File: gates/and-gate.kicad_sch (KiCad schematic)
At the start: 5 parts

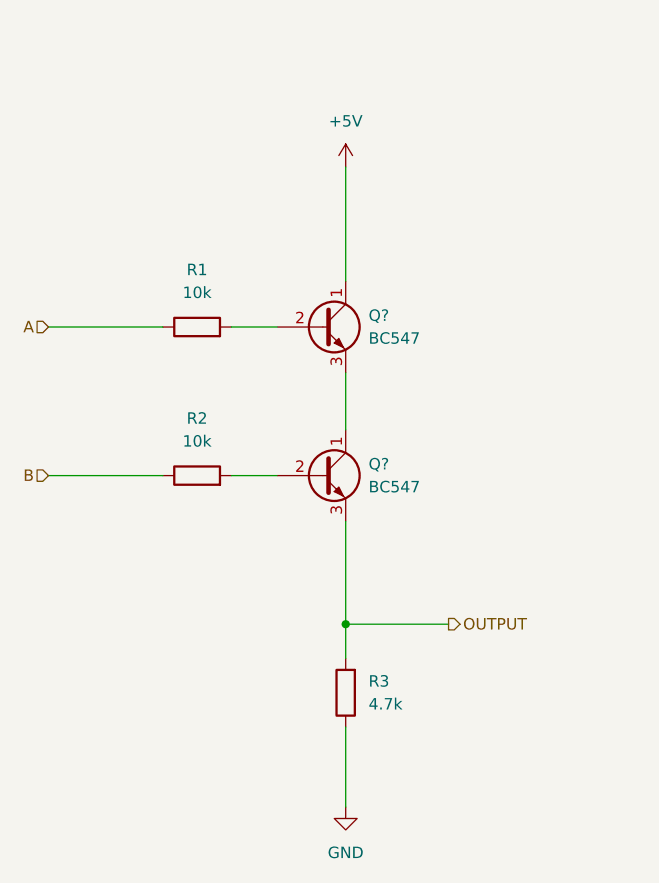
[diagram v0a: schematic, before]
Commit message: replaced circuitry in half adder with reusable gates
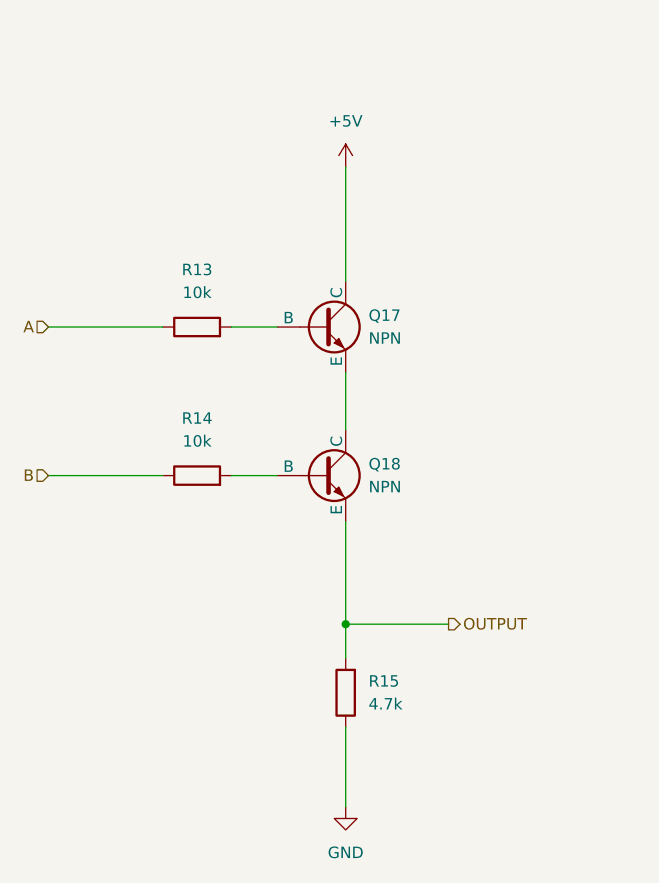
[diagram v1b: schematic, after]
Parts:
- removed Q? (x2): BC547, Package_TO_SOT_THT:TO-92_Inline, symbol Transistor_BJT:BC547
- added Q17, Q18: NPN, symbol Simulation_SPICE:NPN
- renumbered R1 to R13, R2 to R14, R3 to R15
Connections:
- net +5V: now also Q17.1 (C)
- net OUTPUT: now also Q18.3 (E)
- net at R13.2: now also Q17.2 (B)
- net at R14.2: now also Q18.2 (B)
- new net: Q17.3 (E), Q18.1 (C)

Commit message: Clock project
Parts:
- renumbered R13 to R28, R14 to R29, R15 to R30
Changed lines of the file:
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@@
 		(dnp no)
 		(fields_autoplaced yes)
-		(property "Reference" "R15"
+		(property "Reference" "R30"
 			(at 115.57 111.7599 0)
 			(effects
@@
 				(path "/88c27409-0a88-4cf1-8b65-cf7271709e32/c6fa08ba-c5fb-43d8-850f-3e5322725fc3/84309def-b1d1-4d08-9cf0-44a7dcd7d6e9"
 					(reference "R24")
+					(unit 1)
+				)
+			)
+			(project "half-adder"
+				(path "/aa2ffd02-03c7-43f5-905d-233d00be0633/8e657cf9-09ea-4d19-97ba-111b741f01c5/84309def-b1d1-4d08-9cf0-44a7dcd7d6e9"
+					(reference "R30")
 					(unit 1)
 				)
@@
 		(dnp no)
 		(fields_autoplaced yes)
-		(property "Reference" "R14"
+		(property "Reference" "R29"
 			(at 96.52 82.55 90)
 			(effects
@@
 				(path "/88c27409-0a88-4cf1-8b65-cf7271709e32/c6fa08ba-c5fb-43d8-850f-3e5322725fc3/84309def-b1d1-4d08-9cf0-44a7dcd7d6e9"
 					(reference "R23")
+					(unit 1)
+				)
+			)
+			(project "half-adder"
+				(path "/aa2ffd02-03c7-43f5-905d-233d00be0633/8e657cf9-09ea-4d19-97ba-111b741f01c5/84309def-b1d1-4d08-9cf0-44a7dcd7d6e9"
+					(reference "R29")
 					(unit 1)
 				)
@@
 		(dnp no)
 		(fields_autoplaced yes)
-		(property "Reference" "#PWR022"
+		(property "Reference" "#PWR032"
 			(at 113.03 132.08 0)
 			(effects
@@
 				(path "/88c27409-0a88-4cf1-8b65-cf7271709e32/c6fa08ba-c5fb-43d8-850f-3e5322725fc3/84309def-b1d1-4d08-9cf0-44a7dcd7d6e9"
 					(reference "#PWR028")
+					(unit 1)
+				)
+			)
+			(project "half-adder"
+				(path "/aa2ffd02-03c7-43f5-905d-233d00be0633/8e657cf9-09ea-4d19-97ba-111b741f01c5/84309def-b1d1-4d08-9cf0-44a7dcd7d6e9"
+					(reference "#PWR032")
 					(unit 1)
 				)
@@
 				)
 			)
+			(project "half-adder"
+				(path "/aa2ffd02-03c7-43f5-905d-233d00be0633/8e657cf9-09ea-4d19-97ba-111b741f01c5/84309def-b1d1-4d08-9cf0-44a7dcd7d6e9"
+					(reference "Q17")
+					(unit 1)
+				)
+			)
 		)
 	)
@@
 		(dnp no)
 		(fields_autoplaced yes)
-		(property "Reference" "R13"
+		(property "Reference" "R28"
 			(at 96.52 66.04 90)
 			(effects
@@
 				(path "/88c27409-0a88-4cf1-8b65-cf7271709e32/c6fa08ba-c5fb-43d8-850f-3e5322725fc3/84309def-b1d1-4d08-9cf0-44a7dcd7d6e9"
 					(reference "R22")
+					(unit 1)
+				)
+			)
+			(project "half-adder"
+				(path "/aa2ffd02-03c7-43f5-905d-233d00be0633/8e657cf9-09ea-4d19-97ba-111b741f01c5/84309def-b1d1-4d08-9cf0-44a7dcd7d6e9"
+					(reference "R28")
 					(unit 1)
 				)
@@
 		(dnp no)
 		(fields_autoplaced yes)
-		(property "Reference" "#PWR021"
+		(property "Reference" "#PWR031"
 			(at 113.03 58.42 0)
 			(effects
@@
 				(path "/88c27409-0a88-4cf1-8b65-cf7271709e32/c6fa08ba-c5fb-43d8-850f-3e5322725fc3/84309def-b1d1-4d08-9cf0-44a7dcd7d6e9"
 					(reference "#PWR027")
+					(unit 1)
+				)
+			)
+			(project "half-adder"
+				(path "/aa2ffd02-03c7-43f5-905d-233d00be0633/8e657cf9-09ea-4d19-97ba-111b741f01c5/84309def-b1d1-4d08-9cf0-44a7dcd7d6e9"
+					(reference "#PWR031")
 					(unit 1)
 				)
@@
 					(unit 1)
 				)
+			)
+			(project "half-adder"
+				(path "/aa2ffd02-03c7-43f5-905d-233d00be0633/8e657cf9-09ea-4d19-97ba-111b741f01c5/84309def-b1d1-4d08-9cf0-44a7dcd7d6e9"
+					(reference "Q18")
+					(unit 1)
+				)

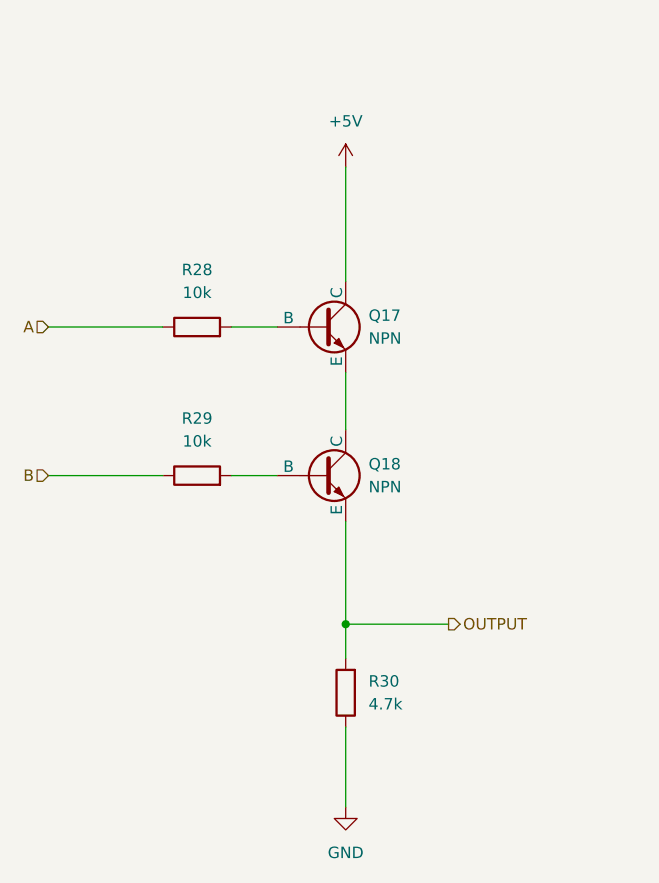
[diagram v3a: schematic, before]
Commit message: Fixed gates and moved half adder to its own directory
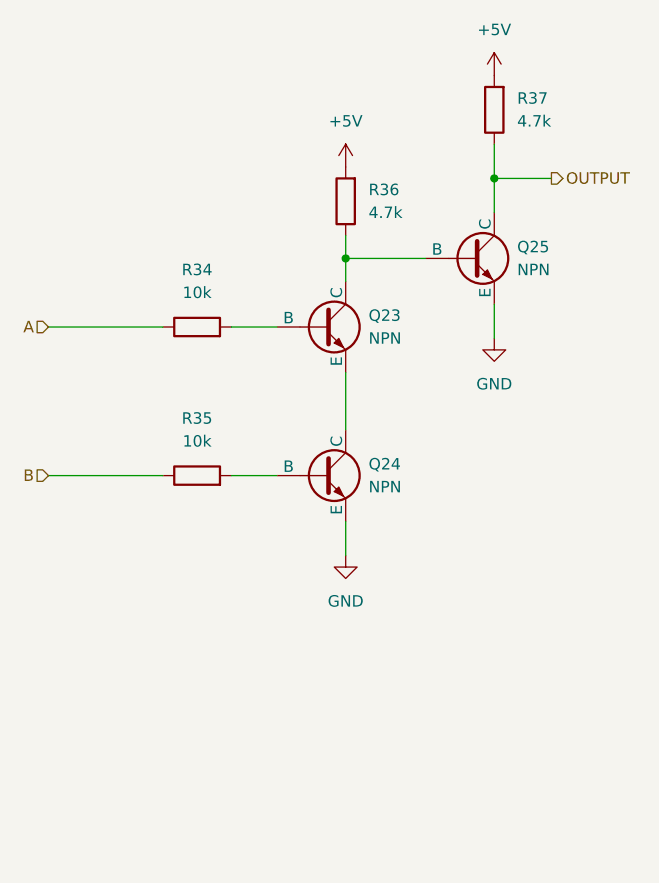
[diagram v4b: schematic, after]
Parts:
- removed R30: 4.7k, symbol Device:R
- added Q25: NPN, symbol Simulation_SPICE:NPN
- added R36, R37: 4.7k, symbol Device:R
- renumbered Q17 to Q23, Q18 to Q24, R28 to R34, R29 to R35
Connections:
- net +5V: now also R36.2, R37.2; no longer Q23.1 (C)
- net GND: now also Q24.3 (E), Q25.3 (E)
- net OUTPUT: now also Q25.1 (C), R37.1; no longer Q24.3 (E)
- new net: Q23.1 (C), Q25.2 (B), R36.1

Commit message: Schematic for register
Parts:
- renumbered Q23 to Q2, Q24 to Q3, Q25 to Q4, R34 to R3, R35 to R4, R36 to R5, R37 to R6
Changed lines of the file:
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@@
 		(dnp no)
 		(fields_autoplaced yes)
-		(property "Reference" "R37"
+		(property "Reference" "R6"
 			(at 132.08 46.9899 0)
 			(effects
@@
 		)
 		(instances
+			(project "register"
+				(path "/176ebc34-d92d-46b0-a9f1-4fb76aa55196/2b210005-c9ef-43dd-bd20-4304cf65b93c/50b17f16-b17e-4be7-91be-701141deb920"
+					(reference "R6")
+					(unit 1)
+				)
+				(path "/176ebc34-d92d-46b0-a9f1-4fb76aa55196/2b210005-c9ef-43dd-bd20-4304cf65b93c/88ab6d81-8ed2-43ff-9a30-e648785f4c69"
+					(reference "R6")
+					(unit 1)
+				)
+			)
 			(project "half-adder"
 				(path "/88c27409-0a88-4cf1-8b65-cf7271709e32/67fd5552-853b-444b-a1e8-d0b78302ff23"
@@
 		(dnp no)
 		(fields_autoplaced yes)
-		(property "Reference" "R35"
+		(property "Reference" "R4"
 			(at 96.52 82.55 90)
 			(effects
@@
 		)
 		(instances
+			(project "register"
+				(path "/176ebc34-d92d-46b0-a9f1-4fb76aa55196/2b210005-c9ef-43dd-bd20-4304cf65b93c/50b17f16-b17e-4be7-91be-701141deb920"
+					(reference "R4")
+					(unit 1)
+				)
+				(path "/176ebc34-d92d-46b0-a9f1-4fb76aa55196/2b210005-c9ef-43dd-bd20-4304cf65b93c/88ab6d81-8ed2-43ff-9a30-e648785f4c69"
+					(reference "R4")
+					(unit 1)
+				)
+			)
 			(project "half-adder"
 				(path "/88c27409-0a88-4cf1-8b65-cf7271709e32/67fd5552-853b-444b-a1e8-d0b78302ff23"
@@
 		(dnp no)
 		(fields_autoplaced yes)
-		(property "Reference" "#PWR044"
+		(property "Reference" "#PWR04"
 			(at 113.03 104.14 0)
 			(effects
@@
 		)
 		(instances
+			(project "register"
+				(path "/176ebc34-d92d-46b0-a9f1-4fb76aa55196/2b210005-c9ef-43dd-bd20-4304cf65b93c/50b17f16-b17e-4be7-91be-701141deb920"
+					(reference "#PWR04")
+					(unit 1)
+				)
+				(path "/176ebc34-d92d-46b0-a9f1-4fb76aa55196/2b210005-c9ef-43dd-bd20-4304cf65b93c/88ab6d81-8ed2-43ff-9a30-e648785f4c69"
+					(reference "#PWR04")
+					(unit 1)
+				)
+			)
 			(project "half-adder"
 				(path "/88c27409-0a88-4cf1-8b65-cf7271709e32/67fd5552-853b-444b-a1e8-d0b78302ff23"
-					(reference "#PWR044")
+					(reference "#PWR042")
 					(unit 1)
 				)
 				(path "/88c27409-0a88-4cf1-8b65-cf7271709e32/e853c8d3-eefb-4fd9-b6d3-3d5bff45301a"
-					(reference "#PWR040")
+					(reference "#PWR038")
 					(unit 1)
 				)
 				(path "/88c27409-0a88-4cf1-8b65-cf7271709e32/9ae6b3ee-29f0-4a20-9e44-32b28e8d9225/84309def-b1d1-4d08-9cf0-44a7dcd7d6e9"
-					(reference "#PWR026")
+					(reference "#PWR024")
 					(unit 1)
 				)
 				(path "/88c27409-0a88-4cf1-8b65-cf7271709e32/c6fa08ba-c5fb-43d8-850f-3e5322725fc3/84309def-b1d1-4d08-9cf0-44a7dcd7d6e9"
-					(reference "#PWR036")
+					(reference "#PWR034")
 					(unit 1)
 				)
@@
 		(dnp no)
 		(fields_autoplaced yes)
-		(property "Reference" "Q23"
+		(property "Reference" "Q2"
 			(at 115.57 71.1199 0)
 			(effects
@@
 		)
 		(instances
+			(project "register"
+				(path "/176ebc34-d92d-46b0-a9f1-4fb76aa55196/2b210005-c9ef-43dd-bd20-4304cf65b93c/50b17f16-b17e-4be7-91be-701141deb920"
+					(reference "Q2")
+					(unit 1)
+				)
+				(path "/176ebc34-d92d-46b0-a9f1-4fb76aa55196/2b210005-c9ef-43dd-bd20-4304cf65b93c/88ab6d81-8ed2-43ff-9a30-e648785f4c69"
+					(reference "Q2")
+					(unit 1)
+				)
+			)
 			(project "half-adder"
 				(path "/88c27409-0a88-4cf1-8b65-cf7271709e32/67fd5552-853b-444b-a1e8-d0b78302ff23"
@@
 		(dnp no)
 		(fields_autoplaced yes)
-		(property "Reference" "#PWR046"
+		(property "Reference" "#PWR06"
 			(at 129.54 80.01 0)
 			(effects
@@
 		)
 		(instances
+			(project "register"
+				(path "/176ebc34-d92d-46b0-a9f1-4fb76aa55196/2b210005-c9ef-43dd-bd20-4304cf65b93c/50b17f16-b17e-4be7-91be-701141deb920"
+					(reference "#PWR06")
+					(unit 1)
+				)
+				(path "/176ebc34-d92d-46b0-a9f1-4fb76aa55196/2b210005-c9ef-43dd-bd20-4304cf65b93c/88ab6d81-8ed2-43ff-9a30-e648785f4c69"
+					(reference "#PWR06")
+					(unit 1)
+				)
+			)
 			(project "half-adder"
 				(path "/88c27409-0a88-4cf1-8b65-cf7271709e32/67fd5552-853b-444b-a1e8-d0b78302ff23"
-					(reference "#PWR046")
+					(reference "#PWR044")
 					(unit 1)
 				)
 				(path "/88c27409-0a88-4cf1-8b65-cf7271709e32/e853c8d3-eefb-4fd9-b6d3-3d5bff45301a"
-					(reference "#PWR042")
+					(reference "#PWR040")
 					(unit 1)
 				)
 				(path "/88c27409-0a88-4cf1-8b65-cf7271709e32/9ae6b3ee-29f0-4a20-9e44-32b28e8d9225/84309def-b1d1-4d08-9cf0-44a7dcd7d6e9"
-					(reference "#PWR028")
+					(reference "#PWR026")
 					(unit 1)
 				)
 				(path "/88c27409-0a88-4cf1-8b65-cf7271709e32/c6fa08ba-c5fb-43d8-850f-3e5322725fc3/84309def-b1d1-4d08-9cf0-44a7dcd7d6e9"
-					(reference "#PWR038")
+					(reference "#PWR036")
 					(unit 1)
 				)
@@
 		(dnp no)
 		(fields_autoplaced yes)
-		(property "Reference" "Q25"
+		(property "Reference" "Q4"
 			(at 132.08 63.4999 0)
 			(effects
@@
 		)
 		(instances
+			(project "register"
+				(path "/176ebc34-d92d-46b0-a9f1-4fb76aa55196/2b210005-c9ef-43dd-bd20-4304cf65b93c/50b17f16-b17e-4be7-91be-701141deb920"
+					(reference "Q4")
+					(unit 1)
+				)
+				(path "/176ebc34-d92d-46b0-a9f1-4fb76aa55196/2b210005-c9ef-43dd-bd20-4304cf65b93c/88ab6d81-8ed2-43ff-9a30-e648785f4c69"
+					(reference "Q4")
+					(unit 1)
+				)
+			)
 			(project "half-adder"
 				(path "/88c27409-0a88-4cf1-8b65-cf7271709e32/67fd5552-853b-444b-a1e8-d0b78302ff23"
@@
 		(dnp no)
 		(fields_autoplaced yes)
-		(property "Reference" "R34"
+		(property "Reference" "R3"
 			(at 96.52 66.04 90)
 			(effects
@@
 		)
 		(instances
+			(project "register"
+				(path "/176ebc34-d92d-46b0-a9f1-4fb76aa55196/2b210005-c9ef-43dd-bd20-4304cf65b93c/50b17f16-b17e-4be7-91be-701141deb920"
+					(reference "R3")
+					(unit 1)
+				)
+				(path "/176ebc34-d92d-46b0-a9f1-4fb76aa55196/2b210005-c9ef-43dd-bd20-4304cf65b93c/88ab6d81-8ed2-43ff-9a30-e648785f4c69"
+					(reference "R3")
+					(unit 1)
+				)
+			)
 			(project "half-adder"
 				(path "/88c27409-0a88-4cf1-8b65-cf7271709e32/67fd5552-853b-444b-a1e8-d0b78302ff23"
@@
 		(dnp no)
 		(fields_autoplaced yes)
-		(property "Reference" "#PWR045"
+		(property "Reference" "#PWR05"
 			(at 129.54 48.26 0)
 			(effects
@@
 		)
 		(instances
+			(project "register"
+				(path "/176ebc34-d92d-46b0-a9f1-4fb76aa55196/2b210005-c9ef-43dd-bd20-4304cf65b93c/50b17f16-b17e-4be7-91be-701141deb920"
+					(reference "#PWR05")
+					(unit 1)
+				)
+				(path "/176ebc34-d92d-46b0-a9f1-4fb76aa55196/2b210005-c9ef-43dd-bd20-4304cf65b93c/88ab6d81-8ed2-43ff-9a30-e648785f4c69"
+					(reference "#PWR05")
+					(unit 1)
+				)
+			)
 			(project "half-adder"
 				(path "/88c27409-0a88-4cf1-8b65-cf7271709e32/67fd5552-853b-444b-a1e8-d0b78302ff23"
-					(reference "#PWR045")
+					(reference "#PWR043")
 					(unit 1)
 				)
 				(path "/88c27409-0a88-4cf1-8b65-cf7271709e32/e853c8d3-eefb-4fd9-b6d3-3d5bff45301a"
-					(reference "#PWR041")
+					(reference "#PWR039")
 					(unit 1)
 				)
 				(path "/88c27409-0a88-4cf1-8b65-cf7271709e32/9ae6b3ee-29f0-4a20-9e44-32b28e8d9225/84309def-b1d1-4d08-9cf0-44a7dcd7d6e9"
-					(reference "#PWR027")
+					(reference "#PWR025")
 					(unit 1)
 				)
 				(path "/88c27409-0a88-4cf1-8b65-cf7271709e32/c6fa08ba-c5fb-43d8-850f-3e5322725fc3/84309def-b1d1-4d08-9cf0-44a7dcd7d6e9"
-					(reference "#PWR037")
+					(reference "#PWR035")
 					(unit 1)
 				)
@@
 		(dnp no)
 		(fields_autoplaced yes)
-		(property "Reference" "#PWR043"
+		(property "Reference" "#PWR03"
 			(at 113.03 58.42 0)
 			(effects
@@
 		)
 		(instances
+			(project "register"
+				(path "/176ebc34-d92d-46b0-a9f1-4fb76aa55196/2b210005-c9ef-43dd-bd20-4304cf65b93c/50b17f16-b17e-4be7-91be-701141deb920"
+					(reference "#PWR03")
+					(unit 1)
+				)
+				(path "/176ebc34-d92d-46b0-a9f1-4fb76aa55196/2b210005-c9ef-43dd-bd20-4304cf65b93c/88ab6d81-8ed2-43ff-9a30-e648785f4c69"
+					(reference "#PWR03")
+					(unit 1)
+				)
+			)
 			(project "half-adder"
 				(path "/88c27409-0a88-4cf1-8b65-cf7271709e32/67fd5552-853b-444b-a1e8-d0b78302ff23"
-					(reference "#PWR043")
+					(reference "#PWR041")
 					(unit 1)
 				)
 				(path "/88c27409-0a88-4cf1-8b65-cf7271709e32/e853c8d3-eefb-4fd9-b6d3-3d5bff45301a"
-					(reference "#PWR039")
+					(reference "#PWR037")
 					(unit 1)
 				)
 				(path "/88c27409-0a88-4cf1-8b65-cf7271709e32/9ae6b3ee-29f0-4a20-9e44-32b28e8d9225/84309def-b1d1-4d08-9cf0-44a7dcd7d6e9"
-					(reference "#PWR025")
+					(reference "#PWR023")
 					(unit 1)
 				)
 				(path "/88c27409-0a88-4cf1-8b65-cf7271709e32/c6fa08ba-c5fb-43d8-850f-3e5322725fc3/84309def-b1d1-4d08-9cf0-44a7dcd7d6e9"
-					(reference "#PWR035")
+					(reference "#PWR033")
 					(unit 1)
 				)
@@
 		(dnp no)
 		(fields_autoplaced yes)
-		(property "Reference" "R36"
+		(property "Reference" "R5"
 			(at 115.57 57.1499 0)
 			(effects
@@
 		)
 		(instances
+			(project "register"
+				(path "/176ebc34-d92d-46b0-a9f1-4fb76aa55196/2b210005-c9ef-43dd-bd20-4304cf65b93c/50b17f16-b17e-4be7-91be-701141deb920"
+					(reference "R5")
+					(unit 1)
+				)
+				(path "/176ebc34-d92d-46b0-a9f1-4fb76aa55196/2b210005-c9ef-43dd-bd20-4304cf65b93c/88ab6d81-8ed2-43ff-9a30-e648785f4c69"
+					(reference "R5")
+					(unit 1)
+				)
+			)
 			(project "half-adder"
 				(path "/88c27409-0a88-4cf1-8b65-cf7271709e32/67fd5552-853b-444b-a1e8-d0b78302ff23"
@@
 		(dnp no)
 		(fields_autoplaced yes)
-		(property "Reference" "Q24"
+		(property "Reference" "Q3"
 			(at 115.57 87.6299 0)
 			(effects
@@
 		)
 		(instances
+			(project "register"
+				(path "/176ebc34-d92d-46b0-a9f1-4fb76aa55196/2b210005-c9ef-43dd-bd20-4304cf65b93c/50b17f16-b17e-4be7-91be-701141deb920"
+					(reference "Q3")
+					(unit 1)
+				)
+				(path "/176ebc34-d92d-46b0-a9f1-4fb76aa55196/2b210005-c9ef-43dd-bd20-4304cf65b93c/88ab6d81-8ed2-43ff-9a30-e648785f4c69"
+					(reference "Q3")
+					(unit 1)
+				)
+			)
 			(project "half-adder"
 				(path "/88c27409-0a88-4cf1-8b65-cf7271709e32/67fd5552-853b-444b-a1e8-d0b78302ff23"

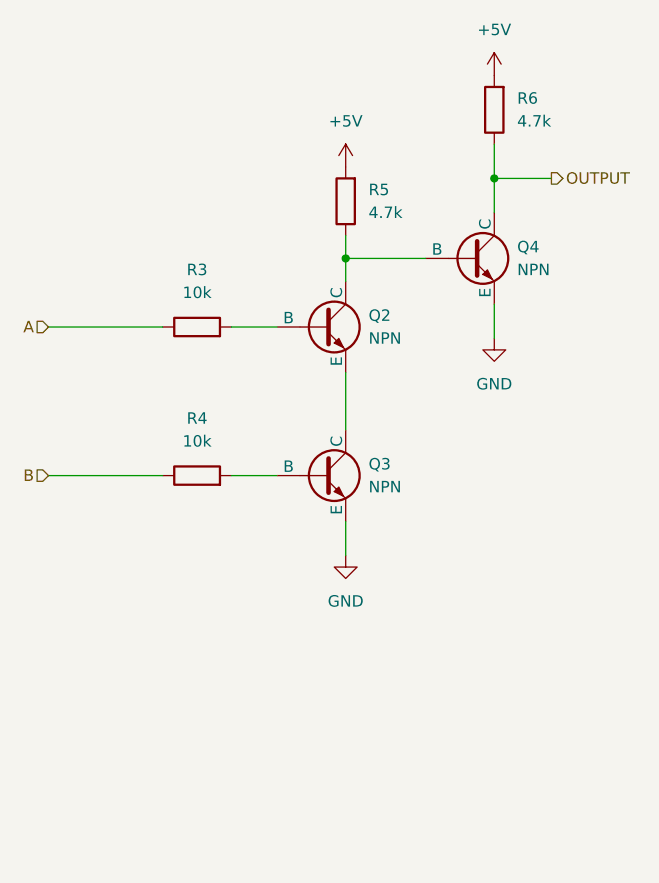
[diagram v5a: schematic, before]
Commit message: Schematic of control-unit
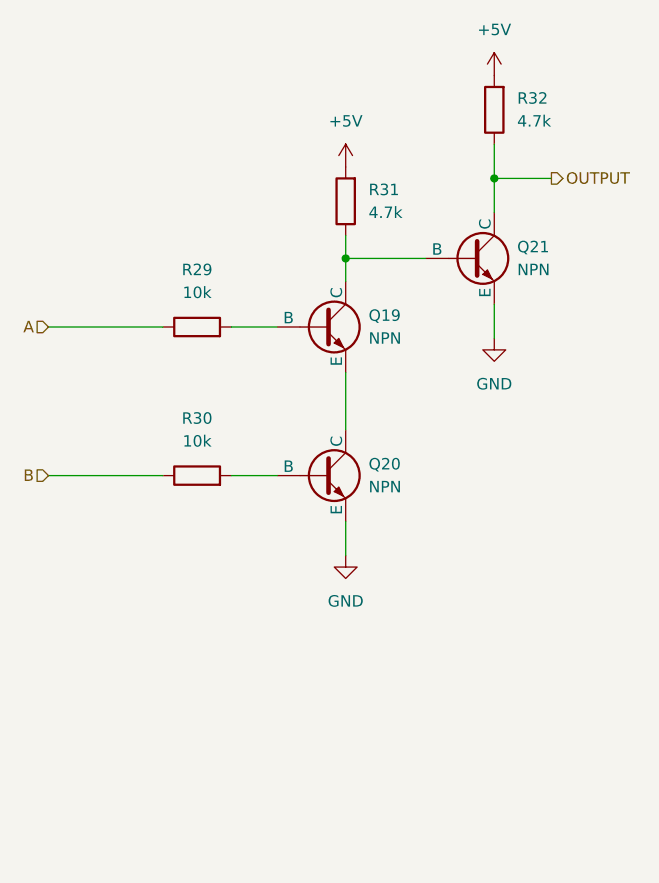
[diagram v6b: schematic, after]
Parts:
- renumbered Q2 to Q19, Q3 to Q20, Q4 to Q21, R3 to R29, R4 to R30, R5 to R31, R6 to R32
